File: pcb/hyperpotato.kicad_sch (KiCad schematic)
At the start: 43 parts, among them J1 Conn_01x02_Socket, J2 Conn_01x03_Pin, Q1 AO3401A, SW1 SW_Push_45deg, SW10 SW_Push_45deg, SW11 SW_Push_45deg, SW12 SW_Push_45deg, SW13 SW_Push_45deg, SW14 SW_SPDT, SW15 SW_Push, SW2 SW_Push_45deg, SW3 SW_Push_45deg, SW4 SW_Push_45deg, SW5 SW_Push_45deg, SW6 SW_Push_45deg, SW7 SW_Push_45deg, SW8 SW_Push_45deg, SW9 SW_Push_45deg, U1 Seeeduino Xiao nRF52840, U2 SK8707-01-SENSOR, U3 SK8707-01, U4 DRV2605LDGS, U5 74HC595

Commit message: wip arrange
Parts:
- D1, D10, D11, D12, D13, D2, D3, D4, D5, D6, D7, D8, D9: footprint ssbb_parts:D_0603_1608Metric_reversible -> ssbb_parts:D_SOD-123_reversible
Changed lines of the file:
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@@
 			)
 		)
-		(property "Footprint" "ssbb_parts:D_0603_1608Metric_reversible"
+		(property "Footprint" "ssbb_parts:D_SOD-123_reversible"
 			(at 73.66 54.61 90)
 			(effects
@@
 			)
 		)
-		(property "Footprint" "ssbb_parts:D_0603_1608Metric_reversible"
+		(property "Footprint" "ssbb_parts:D_SOD-123_reversible"
 			(at 35.56 54.61 90)
 			(effects
@@
 			)
 		)
-		(property "Footprint" "ssbb_parts:D_0603_1608Metric_reversible"
+		(property "Footprint" "ssbb_parts:D_SOD-123_reversible"
 			(at 86.36 54.61 90)
 			(effects
@@
 			)
 		)
-		(property "Footprint" "ssbb_parts:D_0603_1608Metric_reversible"
+		(property "Footprint" "ssbb_parts:D_SOD-123_reversible"
 			(at 86.36 68.58 90)
 			(effects
@@
 			)
 		)
-		(property "Footprint" "ssbb_parts:D_0603_1608Metric_reversible"
+		(property "Footprint" "ssbb_parts:D_SOD-123_reversible"
 			(at 48.26 41.91 90)
 			(effects
@@
 			)
 		)
-		(property "Footprint" "ssbb_parts:D_0603_1608Metric_reversible"
+		(property "Footprint" "ssbb_parts:D_SOD-123_reversible"
 			(at 73.66 68.58 90)
 			(effects
@@
 			)
 		)
-		(property "Footprint" "ssbb_parts:D_0603_1608Metric_reversible"
+		(property "Footprint" "ssbb_parts:D_SOD-123_reversible"
 			(at 48.26 68.58 90)
 			(effects
@@
 			)
 		)
-		(property "Footprint" "ssbb_parts:D_0603_1608Metric_reversible"
+		(property "Footprint" "ssbb_parts:D_SOD-123_reversible"
 			(at 60.96 41.91 90)
 			(effects
@@
 			)
 		)
-		(property "Footprint" "ssbb_parts:D_0603_1608Metric_reversible"
+		(property "Footprint" "ssbb_parts:D_SOD-123_reversible"
 			(at 60.96 54.61 90)
 			(effects
@@
 			)
 		)
-		(property "Footprint" "ssbb_parts:D_0603_1608Metric_reversible"
+		(property "Footprint" "ssbb_parts:D_SOD-123_reversible"
 			(at 86.36 41.91 90)
 			(effects
@@
 			)
 		)
-		(property "Footprint" "ssbb_parts:D_0603_1608Metric_reversible"
+		(property "Footprint" "ssbb_parts:D_SOD-123_reversible"
 			(at 73.66 41.91 90)
 			(effects
@@
 			)
 		)
-		(property "Footprint" "ssbb_parts:D_0603_1608Metric_reversible"
+		(property "Footprint" "ssbb_parts:D_SOD-123_reversible"
 			(at 60.96 68.58 90)
 			(effects
@@
 			)
 		)
-		(property "Footprint" "ssbb_parts:D_0603_1608Metric_reversible"
+		(property "Footprint" "ssbb_parts:D_SOD-123_reversible"
 			(at 48.26 54.61 90)
 			(effects

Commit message: Wire everything except the mcu
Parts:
- U2: footprint ssbb_parts:Sprintek_SK8707-01_Sensor -> ssbb_parts:Sprintek_SK8707-01_Sensor_reversible
- U3: footprint (none) -> ssbb_parts:Sprintek_SK8707-01_reversible
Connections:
- net ROW1: no longer D10.1 (K), D11.1 (K), D12.1 (K), D13.1 (K), D5.2 (A), SW5.2
- net ROW2: now also D10.1 (K), D11.1 (K), D12.1 (K), D13.1 (K)
- new net: D5.2 (A), SW5.2
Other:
- moved on the sheet: R4, R5
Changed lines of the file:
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@@
 	)
 	(junction
-		(at 35.56 52.07)
-		(diameter 0)
-		(color 0 0 0 0)
-	)
-	(junction
 		(at 60.96 44.45)
 		(diameter 0)
@@
 	(wire
 		(pts
-			(xy 35.56 57.15) (xy 35.56 52.07)
-		)
-		(stroke
-			(width 0)
-			(type default)
-		)
-	)
-	(wire
-		(pts
 			(xy 27.94 116.84) (xy 26.67 116.84)
 		)
@@
 		)
 	)
-	(global_label "ROW1"
+	(global_label "ROW2"
 		(shape input)
 		(at 26.67 71.12 180)
@@
 	(global_label "TP_CLK"
 		(shape input)
-		(at 218.44 142.24 270)
+		(at 222.25 142.24 270)
 		(fields_autoplaced yes)
 		(effects
@@
 		)
 		(property "Intersheetrefs" "${INTERSHEET_REFS}"
-			(at 218.44 151.9985 90)
+			(at 222.25 151.9985 90)
 			(effects
 				(font
@@
 	(global_label "TP_DATA"
 		(shape input)
-		(at 204.47 142.24 270)
+		(at 208.28 142.24 270)
 		(fields_autoplaced yes)
 		(effects
@@
 		)
 		(property "Intersheetrefs" "${INTERSHEET_REFS}"
-			(at 204.47 152.8452 90)
+			(at 208.28 152.8452 90)
 			(effects
 				(font
@@
 			)
 		)
-		(property "Description" ""
+		(property "Description" "Power symbol creates a global label with name \"GND\" , ground"
 			(at 182.88 212.09 0)
 			(effects
@@
 			)
 		)
-		(property "Description" ""
+		(property "Description" "Power symbol creates a global label with name \"VCC\""
 			(at 193.04 175.26 0)
 			(effects
@@
 	(symbol
 		(lib_id "ssbb_parts:+3.3V_OPTIONAL")
-		(at 218.44 137.16 0)
+		(at 222.25 137.16 0)
 		(unit 1)
 		(exclude_from_sim no)
@@
 		(fields_autoplaced yes)
 		(property "Reference" "#PWR020"
-			(at 218.44 140.97 0)
+			(at 222.25 140.97 0)
 			(effects
 				(font
@@
 		)
 		(property "Value" "+3.3V_OPTIONAL"
-			(at 218.44 132.08 0)
+			(at 222.25 132.08 0)
 			(effects
 				(font
@@
 		)
 		(property "Footprint" ""
-			(at 218.44 137.16 0)
+			(at 222.25 137.16 0)
 			(effects
 				(font
@@
 		)
 		(property "Datasheet" ""
-			(at 218.44 137.16 0)
+			(at 222.25 137.16 0)
 			(effects
 				(font
@@
 		)
 		(property "Description" "Power symbol creates a global label with name \"+3.3V_OPTIONAL\""
-			(at 218.44 137.16 0)
+			(at 222.25 137.16 0)
 			(effects
 				(font
@@
 			)
 		)
-		(property "Footprint" "ssbb_parts:Sprintek_SK8707-01_Sensor"
+		(property "Footprint" "ssbb_parts:Sprintek_SK8707-01_Sensor_reversible"
 			(at 125.73 190.5 0)
 			(effects
@@
 	(symbol
 		(lib_id "Device:R_Small")
-		(at 204.47 139.7 0)
+		(at 208.28 139.7 0)
 		(unit 1)
 		(exclude_from_sim no)
@@
 		(fields_autoplaced yes)
 		(property "Reference" "R4"
-			(at 207.01 138.4299 0)
+			(at 210.82 138.4299 0)
 			(effects
 				(font
@@
 		)
 		(property "Value" "R_Small"
-			(at 207.01 140.9699 0)
+			(at 210.82 140.9699 0)
 			(effects
 				(font
@@
 		)
 		(property "Footprint" "ssbb_parts:R_0603_1608Metric_reversible"
-			(at 204.47 139.7 0)
+			(at 208.28 139.7 0)
 			(effects
 				(font
@@
 		)
 		(property "Datasheet" "~"
-			(at 204.47 139.7 0)
+			(at 208.28 139.7 0)
 			(effects
 				(font
@@
 		)
 		(property "Description" "Resistor, small symbol"
-			(at 204.47 139.7 0)
+			(at 208.28 139.7 0)
 			(effects
 				(font
@@
 			)
 		)
-		(property "Footprint" ""
+		(property "Footprint" "ssbb_parts:Sprintek_SK8707-01_reversible"
 			(at 125.73 161.29 0)
 			(effects
@@
 	(symbol
 		(lib_id "Device:R_Small")
-		(at 218.44 139.7 0)
+		(at 222.25 139.7 0)
 		(unit 1)
 		(exclude_from_sim no)
@@
 		(fields_autoplaced yes)
 		(property "Reference" "R5"
-			(at 220.98 138.4299 0)
+			(at 224.79 138.4299 0)
 			(effects
 				(font
@@
 		)
 		(property "Value" "R_Small"
-			(at 220.98 140.9699 0)
+			(at 224.79 140.9699 0)
 			(effects
 				(font
@@
 		)
 		(property "Footprint" "ssbb_parts:R_0603_1608Metric_reversible"
-			(at 218.44 139.7 0)
+			(at 222.25 139.7 0)
 			(effects
 				(font
@@
 		)
 		(property "Datasheet" "~"
-			(at 218.44 139.7 0)
+			(at 222.25 139.7 0)
 			(effects
 				(font
@@
 		)
 		(property "Description" "Resistor, small symbol"
-			(at 218.44 139.7 0)
+			(at 222.25 139.7 0)
 			(effects
 				(font
@@
 	(symbol
 		(lib_id "ssbb_parts:+3.3V_OPTIONAL")
-		(at 204.47 137.16 0)
+		(at 208.28 137.16 0)
 		(unit 1)
 		(exclude_from_sim no)
@@
 		(fields_autoplaced yes)
 		(property "Reference" "#PWR019"
-			(at 204.47 140.97 0)
+			(at 208.28 140.97 0)
 			(effects
 				(font
@@
 		)
 		(property "Value" "+3.3V_OPTIONAL"
-			(at 204.47 132.08 0)
+			(at 208.28 132.08 0)
 			(effects
 				(font
@@
 		)
 		(property "Footprint" ""
-			(at 204.47 137.16 0)
+			(at 208.28 137.16 0)
 			(effects
 				(font
@@
 		)
 		(property "Datasheet" ""
-			(at 204.47 137.16 0)
+			(at 208.28 137.16 0)
 			(effects
 				(font
@@
 		)
 		(property "Description" "Power symbol creates a global label with name \"+3.3V_OPTIONAL\""
-			(at 204.47 137.16 0)
+			(at 208.28 137.16 0)
 			(effects
 				(font
@@
 			)
 		)
-		(property "Description" ""
+		(property "Description" "8-bit serial in/out Shift Register 3-State Outputs"
 			(at 193.04 193.04 0)
 			(effects

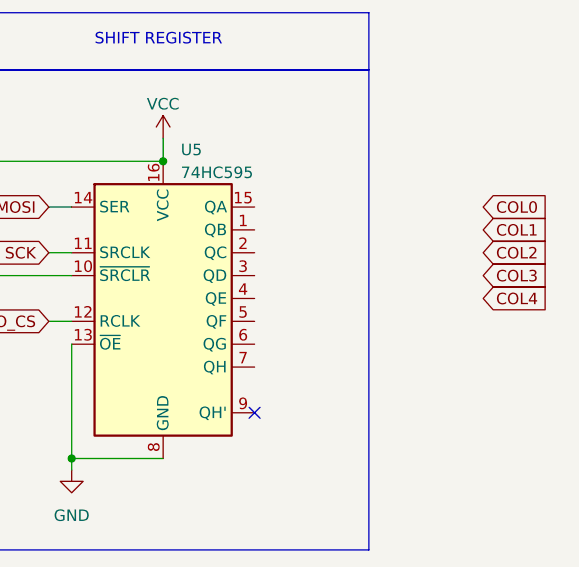
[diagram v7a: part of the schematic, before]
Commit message: Wire shift register
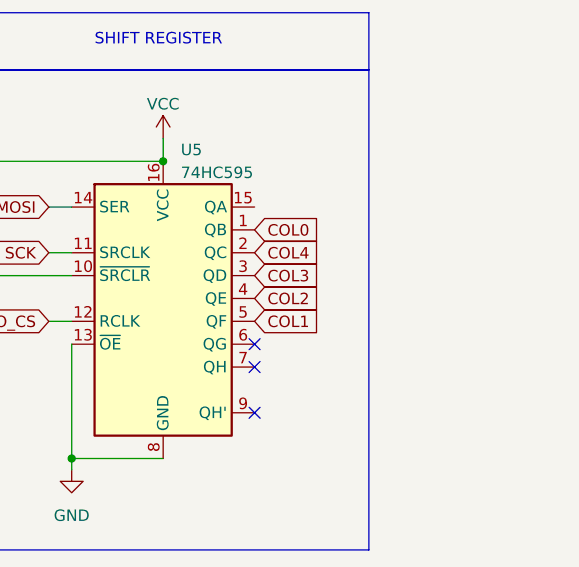
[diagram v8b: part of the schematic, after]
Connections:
- net COL0: now also U5.1 (QB)
- net COL1: now also U5.5 (QF)
- net COL2: now also U5.4 (QE)
- net COL3: now also U5.3 (QD)
- net COL4: now also U5.2 (QC)
- no-connect marks 9 -> 11
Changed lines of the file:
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@@
+	)
+	(no_connect
+		(at 203.2 200.66)
+	)
+	(no_connect
+		(at 203.2 198.12)
 	)
 	(no_connect
@@
 	(global_label "COL2"
 		(shape input)
-		(at 228.6 187.96 0)
-		(fields_autoplaced yes)
-		(effects
-			(font
-				(size 1.27 1.27)
-			)
-			(justify left)
-		)
-		(property "Intersheetrefs" "${INTERSHEET_REFS}"
-			(at 236.3439 187.96 0)
+		(at 203.2 193.04 0)
+		(fields_autoplaced yes)
+		(effects
+			(font
+				(size 1.27 1.27)
+			)
+			(justify left)
+		)
+		(property "Intersheetrefs" "${INTERSHEET_REFS}"
+			(at 210.9439 193.04 0)
 			(effects
 				(font
@@
 	(global_label "COL4"
 		(shape input)
-		(at 228.6 193.04 0)
-		(fields_autoplaced yes)
-		(effects
-			(font
-				(size 1.27 1.27)
-			)
-			(justify left)
-		)
-		(property "Intersheetrefs" "${INTERSHEET_REFS}"
-			(at 236.4233 193.04 0)
+		(at 203.2 187.96 0)
+		(fields_autoplaced yes)
+		(effects
+			(font
+				(size 1.27 1.27)
+			)
+			(justify left)
+		)
+		(property "Intersheetrefs" "${INTERSHEET_REFS}"
+			(at 211.0233 187.96 0)
 			(effects
 				(font
@@
 	(global_label "COL0"
 		(shape input)
-		(at 228.6 182.88 0)
-		(fields_autoplaced yes)
-		(effects
-			(font
-				(size 1.27 1.27)
-			)
-			(justify left)
-		)
-		(property "Intersheetrefs" "${INTERSHEET_REFS}"
-			(at 236.3439 182.88 0)
+		(at 203.2 185.42 0)
+		(fields_autoplaced yes)
+		(effects
+			(font
+				(size 1.27 1.27)
+			)
+			(justify left)
+		)
+		(property "Intersheetrefs" "${INTERSHEET_REFS}"
+			(at 210.9439 185.42 0)
 			(effects
 				(font
@@
 	(global_label "COL1"
 		(shape input)
-		(at 228.6 185.42 0)
-		(fields_autoplaced yes)
-		(effects
-			(font
-				(size 1.27 1.27)
-			)
-			(justify left)
-		)
-		(property "Intersheetrefs" "${INTERSHEET_REFS}"
-			(at 236.3439 185.42 0)
+		(at 203.2 195.58 0)
+		(fields_autoplaced yes)
+		(effects
+			(font
+				(size 1.27 1.27)
+			)
+			(justify left)
+		)
+		(property "Intersheetrefs" "${INTERSHEET_REFS}"
+			(at 210.9439 195.58 0)
 			(effects
 				(font
@@
 	(global_label "COL3"
 		(shape input)
-		(at 228.6 190.5 0)
-		(fields_autoplaced yes)
-		(effects
-			(font
-				(size 1.27 1.27)
-			)
-			(justify left)
-		)
-		(property "Intersheetrefs" "${INTERSHEET_REFS}"
-			(at 236.4233 190.5 0)
-			(effects
-				(font
+		(at 203.2 190.5 0)
+		(fields_autoplaced yes)
+		(effects
+			(font
+				(size 1.27 1.27)
+			)
+			(justify left)
+		)
+		(property "Intersheetrefs" "${INTERSHEET_REFS}"
+			(at 211.0233 190.5 0)
+			(effects
+				(font
